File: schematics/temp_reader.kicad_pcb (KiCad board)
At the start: 2 copper layers, 54.5 x 53 mm, 11 parts, among them Q1 2N3904, Q2 2N3904, Q3 2N3904, U1 7-seg, U2 7-seg, U3 7-seg, U4 AM2320, U5 MG90S_servo

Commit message: added tempurature module
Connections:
- A1 pad 13: Net-(A1-D10) -> unconnected-(A1-D10-Pad13)
- A1 pad 2: Net-(A1-RX1) -> unconnected-(A1-RX1-Pad2)
- A1 pad 23: unconnected-(A1-SDA/A4-Pad23) -> SDA
- A1 pad 24: unconnected-(A1-SCL/A5-Pad24) -> SCL
- R1 pad 1: Net-(A1-D9) -> SCL
- R2 pad 1: Net-(A1-D10) -> SDA
- U4 pad 2: Net-(A1-D10) -> SDA
- U4 pad 4: Net-(A1-D9) -> SCL
- U5 pad 3: Net-(A1-RX1) -> Net-(A1-D9)
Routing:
- net Net-(A1-D10): track 81.5 -> 0.00 mm
- net SDA: track 0.00 -> 80.8 mm
- net SCL: track 0.00 -> 77.7 mm
- net Net-(A1-RX1): track 39.0 -> 0.00 mm
- net Net-(A1-D9): track 81.8 -> 72.0 mm
- net +5V: track 82.5 -> 84.6 mm, vias 3 -> 2
- net GND: track 87.0 -> 87.9 mm

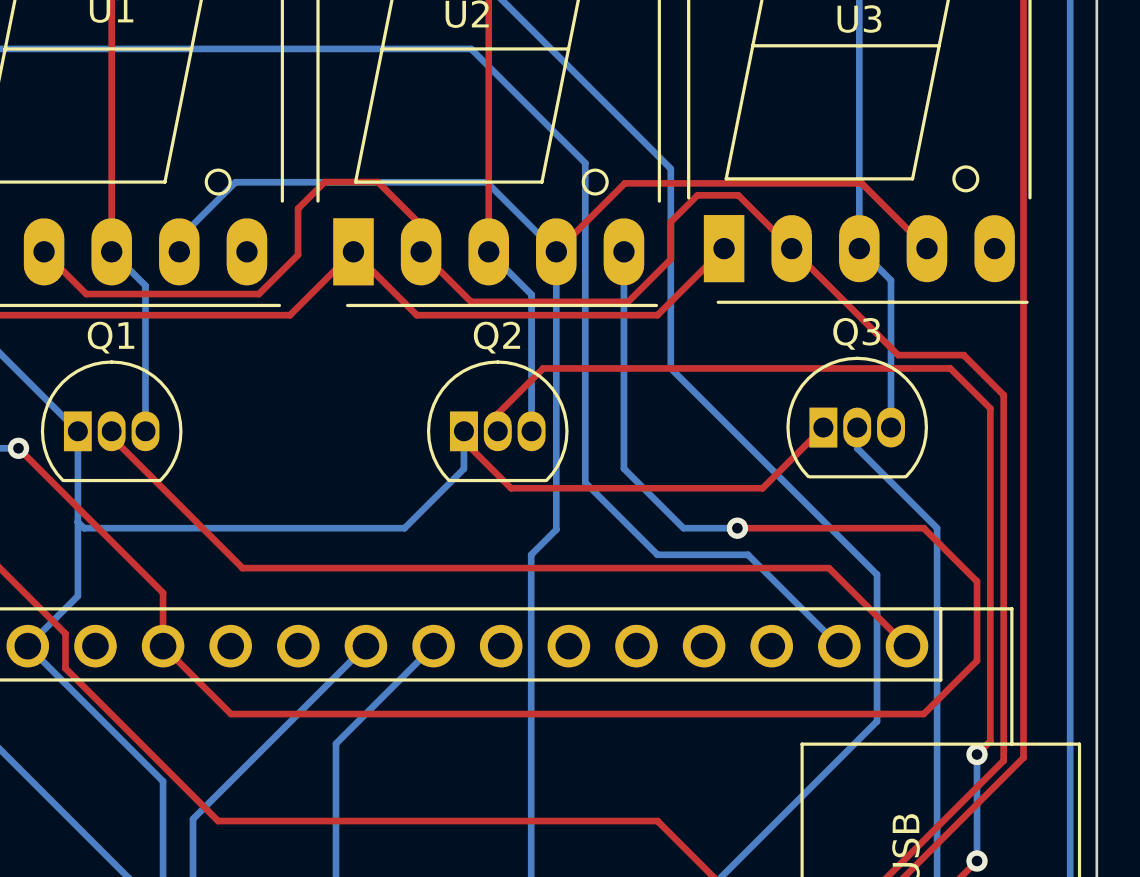
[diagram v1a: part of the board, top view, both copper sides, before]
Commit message: using 3.3v for decimal LED
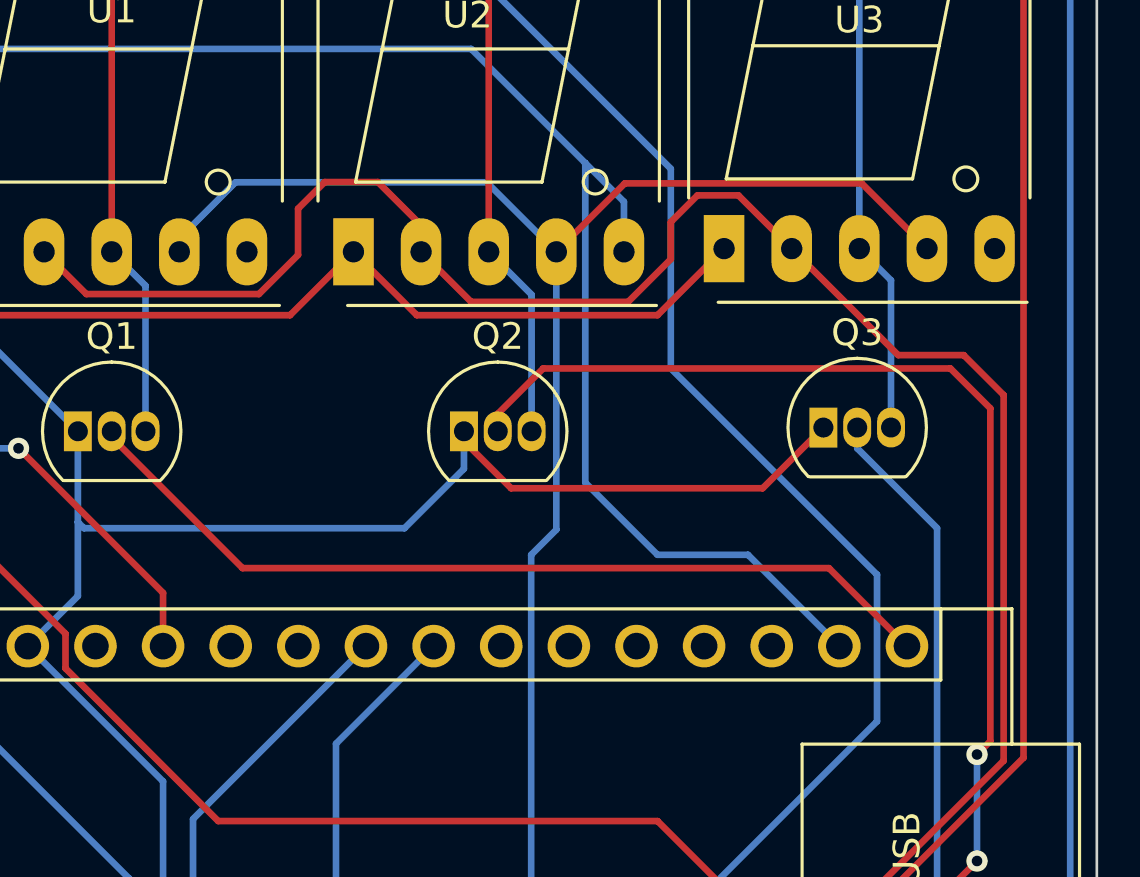
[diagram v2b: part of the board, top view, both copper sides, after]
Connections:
- U2 pad 5: +5V -> +3.3V
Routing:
- net +5V: track 84.6 -> 26.0 mm, vias 2 -> 1
- net +3.3V: track 87.3 -> 91.2 mm
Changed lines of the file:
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@@
       (net 23 "vbr") (pinfunction "vbr") (pintype "input"))
     (pad "5" thru_hole oval (at 0 10.16) (size 1.524 2.524) (drill 0.8) (layers "*.Cu" "*.Mask")
-      (net 26 "+5V") (pinfunction "DP") (pintype "input"))
+      (net 27 "+3.3V") (pinfunction "DP") (pintype "input"))
     (pad "6" thru_hole oval (at 15.24 10.16) (size 1.524 2.524) (drill 0.8) (layers "*.Cu" "*.Mask")
       (net 30 "vtr") (pinfunction "vtr") (pintype "input"))
@@
   (segment (start 145.58 76.62) (end 147.96 79) (width 0.25) (layer "F.Cu") (net 25))
   (segment (start 152.5 107.5) (end 153 108) (width 0.25) (layer "F.Cu") (net 25))
-  (segment (start 169 91.98) (end 169 89) (width 0.25) (layer "F.Cu") (net 26))
   (segment (start 138.43 89.43) (end 133 84) (width 0.25) (layer "F.Cu") (net 26))
-  (segment (start 140.98 93.98) (end 167 93.98) (width 0.25) (layer "F.Cu") (net 26))
   (segment (start 138.43 91.43) (end 138.43 89.43) (width 0.25) (layer "F.Cu") (net 26))
-  (segment (start 167 93.98) (end 169 91.98) (width 0.25) (layer "F.Cu") (net 26))
-  (segment (start 169 89) (end 167 87) (width 0.25) (layer "F.Cu") (net 26))
-  (segment (start 138.43 91.43) (end 140.98 93.98) (width 0.25) (layer "F.Cu") (net 26))
-  (segment (start 160 87) (end 167 87) (width 0.25) (layer "F.Cu") (net 26))
   (via (at 133 84) (size 0.8) (drill 0.4) (layers "F.Cu" "B.Cu") (net 26))
-  (via (at 160 87) (size 0.8) (drill 0.4) (layers "F.Cu" "B.Cu") (net 26))
   (segment (start 122.925 81.925) (end 122.925 78.075) (width 0.25) (layer "B.Cu") (net 26))
   (segment (start 122.925 78.075) (end 124 77) (width 0.25) (layer "B.Cu") (net 26))
-  (segment (start 155.74 76.62) (end 155.74 84.765305) (width 0.25) (layer "B.Cu") (net 26))
   (segment (start 133 84) (end 125 84) (width 0.25) (layer "B.Cu") (net 26))
   (segment (start 125 84) (end 122.925 81.925) (width 0.25) (layer "B.Cu") (net 26))
-  (segment (start 160 87) (end 158 87) (width 0.25) (layer "B.Cu") (net 26))
-  (segment (start 155.74 84.765305) (end 157.974695 87) (width 0.25) (layer "B.Cu") (net 26))
   (segment (start 123 85.5) (end 122 84.5) (width 0.25) (layer "F.Cu") (net 27))
   (segment (start 124.075 96.425) (end 124.075 88.075) (width 0.25) (layer "F.Cu") (net 27))
@@
   (segment (start 150 69) (end 154.287 73.287) (width 0.25) (layer "B.Cu") (net 27))
   (segment (start 154.287 85.287) (end 157 88) (width 0.25) (layer "B.Cu") (net 27))
+  (segment (start 154.287 73.287) (end 155.74 74.74) (width 0.25) (layer "B.Cu") (net 27))
   (segment (start 157 88) (end 160.4 88) (width 0.25) (layer "B.Cu") (net 27))
+  (segment (start 155.74 74.74) (end 155.74 76.62) (width 0.25) (layer "B.Cu") (net 27))
   (segment (start 160.4 88) (end 163.83 91.43) (width 0.25) (layer "B.Cu") (net 27))
   (segment (start 124 69) (end 150 69) (width 0.25) (layer "B.Cu") (net 27))

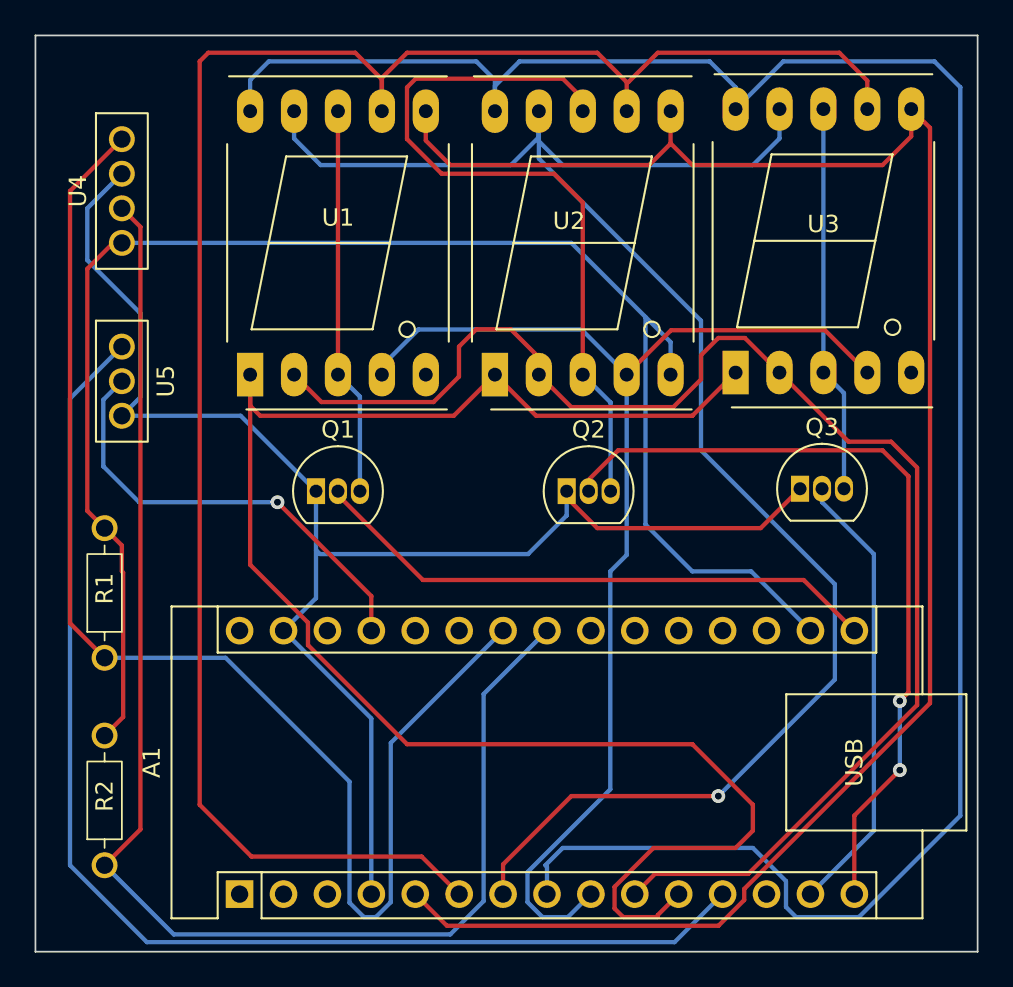
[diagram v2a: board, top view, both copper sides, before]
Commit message: updated servo model and adjusted temp sensor blueprint
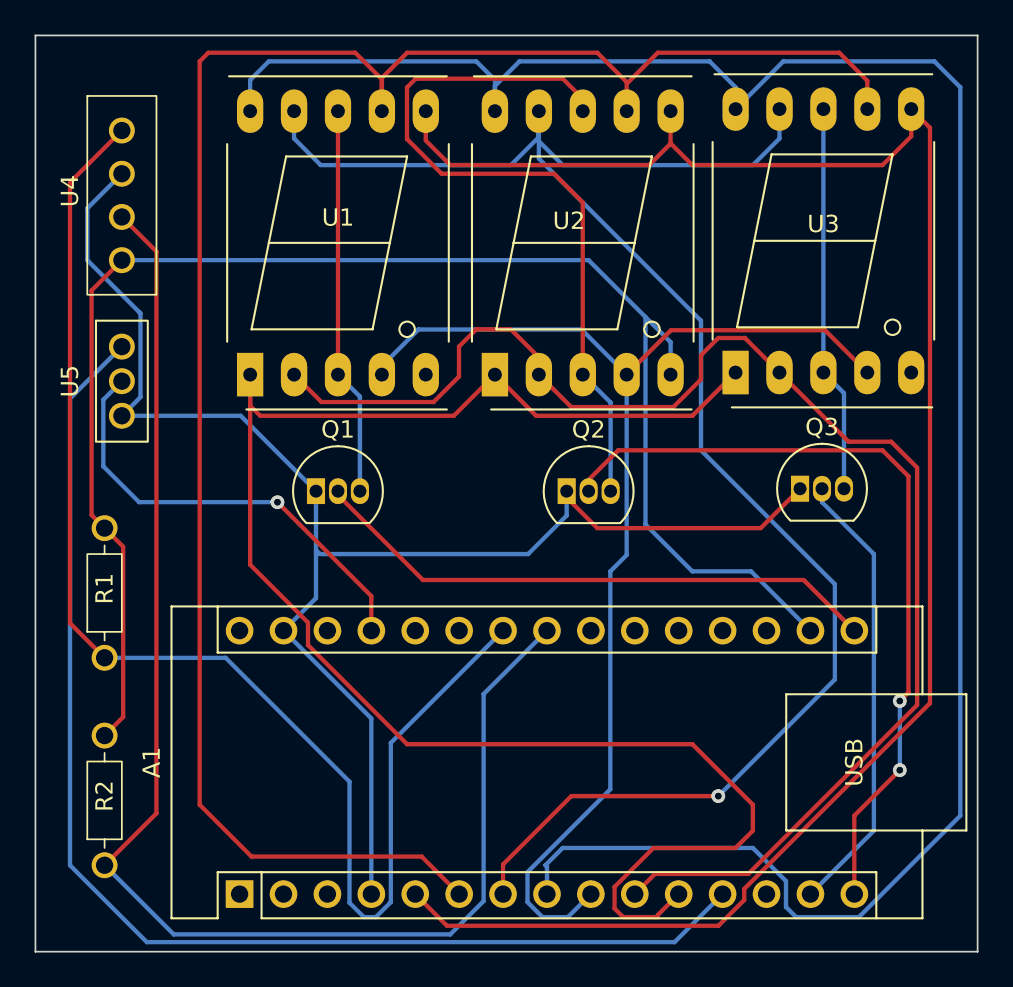
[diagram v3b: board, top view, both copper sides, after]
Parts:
- U5: value MG90S_servo -> SG90_servo
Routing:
- net +3.3V: track 91.2 -> 89.1 mm
- net SCL: track 77.7 -> 78.2 mm
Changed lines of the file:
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@@
     (property "Sheetname" "")
     (attr through_hole)
-    (fp_text reference "U5" (at 0 2.54 90 unlocked) (layer "F.SilkS")
-        (effects (font (size 1 1) (thickness 0.15)))
-    )
-    (fp_text value "MG90S_servo" (at 0 -2.5 90 unlocked) (layer "F.Fab")
+    (fp_text reference "U5" (at 0 -3 90 unlocked) (layer "F.SilkS")
+        (effects (font (size 1 1) (thickness 0.15)))
+    )
+    (fp_text value "SG90_servo" (at 0 -2.5 90 unlocked) (layer "F.Fab")
         (effects (font (size 1 1) (thickness 0.15)))
     )
@@
     (property "Sheetname" "")
     (attr through_hole)
-    (fp_text reference "U4" (at 0 -2.54 90 unlocked) (layer "F.SilkS")
+    (fp_text reference "U4" (at 0 -3 90 unlocked) (layer "F.SilkS")
         (effects (font (size 1 1) (thickness 0.15)))
     )
@@
         (effects (font (size 1 1) (thickness 0.15)))
     )
-    (fp_rect (start 4.5 -1.5) (end -4.5 1.5)
-      (stroke (width 0.12) (type solid)) (fill none) (layer "F.SilkS"))
-    (pad "1" thru_hole circle (at -3 0 90) (size 1.5 1.5) (drill 1) (layers "*.Cu" "*.Mask")
+    (fp_rect (start 5.5 -2) (end -6 2)
+      (stroke (width 0.1) (type default)) (fill none) (layer "F.SilkS"))
+    (pad "1" thru_hole circle (at -4 0 90) (size 1.5 1.5) (drill 1) (layers "*.Cu" "*.Mask")
       (net 27 "+3.3V") (pinfunction "V+") (pintype "input"))
-    (pad "2" thru_hole circle (at -1 0 90) (size 1.5 1.5) (drill 1) (layers "*.Cu" "*.Mask")
+    (pad "2" thru_hole circle (at -1.5 0 90) (size 1.5 1.5) (drill 1) (layers "*.Cu" "*.Mask")
       (net 11 "SDA") (pinfunction "SDA") (pintype "input"))
     (pad "3" thru_hole circle (at 1 0 90) (size 1.5 1.5) (drill 1) (layers "*.Cu" "*.Mask")
       (net 18 "GND") (pinfunction "GND") (pintype "input"))
-    (pad "4" thru_hole circle (at 3 0 90) (size 1.5 1.5) (drill 1) (layers "*.Cu" "*.Mask")
+    (pad "4" thru_hole circle (at 3.5 0 90) (size 1.5 1.5) (drill 1) (layers "*.Cu" "*.Mask")
       (net 12 "SCL") (pinfunction "SCL") (pintype "input"))
   )
@@
   (segment (start 121 105) (end 121 78) (width 0.25) (layer "B.Cu") (net 4))
   (segment (start 125.45 109.45) (end 121 105) (width 0.25) (layer "B.Cu") (net 4))
-  (segment (start 123 105) (end 125.075 102.925) (width 0.25) (layer "F.Cu") (net 11))
-  (segment (start 125.075 102.925) (end 125.075 68.075) (width 0.25) (layer "F.Cu") (net 11))
-  (segment (start 125.075 68.075) (end 124 67) (width 0.25) (layer "F.Cu") (net 11))
+  (segment (start 124 67.5) (end 126 69.5) (width 0.25) (layer "F.Cu") (net 11))
+  (segment (start 123 105) (end 126 102) (width 0.25) (layer "F.Cu") (net 11))
+  (segment (start 126 69.5) (end 126 102) (width 0.25) (layer "F.Cu") (net 11))
   (segment (start 144.925 95.095) (end 144.925 107.075) (width 0.25) (layer "B.Cu") (net 11))
   (segment (start 127 109) (end 123 105) (width 0.25) (layer "B.Cu") (net 11))
@@
   (segment (start 143 109) (end 127 109) (width 0.25) (layer "B.Cu") (net 11))
   (segment (start 148.59 91.43) (end 144.925 95.095) (width 0.25) (layer "B.Cu") (net 11))
-  (segment (start 124 63) (end 121 66) (width 0.25) (layer "F.Cu") (net 12))
+  (segment (start 121 65.5) (end 121 91) (width 0.25) (layer "F.Cu") (net 12))
+  (segment (start 124 62.5) (end 121 65.5) (width 0.25) (layer "F.Cu") (net 12))
   (segment (start 121 91) (end 123 93) (width 0.25) (layer "F.Cu") (net 12))
-  (segment (start 121 66) (end 121 91) (width 0.25) (layer "F.Cu") (net 12))
   (segment (start 139.555 97.925) (end 146.05 91.43) (width 0.25) (layer "B.Cu") (net 12))
   (segment (start 138 108) (end 138.690991 108) (width 0.25) (layer "B.Cu") (net 12))
@@
   (segment (start 133 84) (end 125 84) (width 0.25) (layer "B.Cu") (net 26))
   (segment (start 125 84) (end 122.925 81.925) (width 0.25) (layer "B.Cu") (net 26))
-  (segment (start 123 85.5) (end 122 84.5) (width 0.25) (layer "F.Cu") (net 27))
-  (segment (start 124.075 96.425) (end 124.075 88.075) (width 0.25) (layer "F.Cu") (net 27))
+  (segment (start 124 70) (end 122.25 71.75) (width 0.25) (layer "F.Cu") (net 27))
+  (segment (start 122.25 71.75) (end 122.25 84.75) (width 0.25) (layer "F.Cu") (net 27))
+  (segment (start 124.075 86.575) (end 123 85.5) (width 0.25) (layer "F.Cu") (net 27))
+  (segment (start 122.25 84.75) (end 123 85.5) (width 0.25) (layer "F.Cu") (net 27))
+  (segment (start 124.075 96.425) (end 124.075 86.575) (width 0.25) (layer "F.Cu") (net 27))
   (segment (start 123 97.5) (end 124.075 96.425) (width 0.25) (layer "F.Cu") (net 27))
-  (segment (start 122 84.5) (end 122 70.5) (width 0.25) (layer "F.Cu") (net 27))
-  (segment (start 124 88) (end 124 86.5) (width 0.25) (layer "F.Cu") (net 27))
-  (segment (start 124 86.5) (end 123 85.5) (width 0.25) (layer "F.Cu") (net 27))
-  (segment (start 122 70.5) (end 124 68.5) (width 0.25) (layer "F.Cu") (net 27))
-  (segment (start 124.075 88.075) (end 124 88) (width 0.25) (layer "F.Cu") (net 27))
-  (segment (start 150 69) (end 154.287 73.287) (width 0.25) (layer "B.Cu") (net 27))
   (segment (start 154.287 85.287) (end 157 88) (width 0.25) (layer "B.Cu") (net 27))
   (segment (start 154.287 73.287) (end 155.74 74.74) (width 0.25) (layer "B.Cu") (net 27))
@@
   (segment (start 155.74 74.74) (end 155.74 76.62) (width 0.25) (layer "B.Cu") (net 27))
   (segment (start 160.4 88) (end 163.83 91.43) (width 0.25) (layer "B.Cu") (net 27))
-  (segment (start 124 69) (end 150 69) (width 0.25) (layer "B.Cu") (net 27))
+  (segment (start 154.287 73.287) (end 151 70) (width 0.25) (layer "B.Cu") (net 27))
   (segment (start 154.287 73.287) (end 154.287 85.287) (width 0.25) (layer "B.Cu") (net 27))
+  (segment (start 151 70) (end 124 70) (width 0.25) (layer "B.Cu") (net 27))
   (segment (start 142.5 65) (end 149 65) (width 0.25) (layer "F.Cu") (net 28))
   (segment (start 149 65) (end 150.66 66.66) (width 0.25) (layer "F.Cu") (net 28))

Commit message: reorganized PCB layout to move sensor farther away from displays
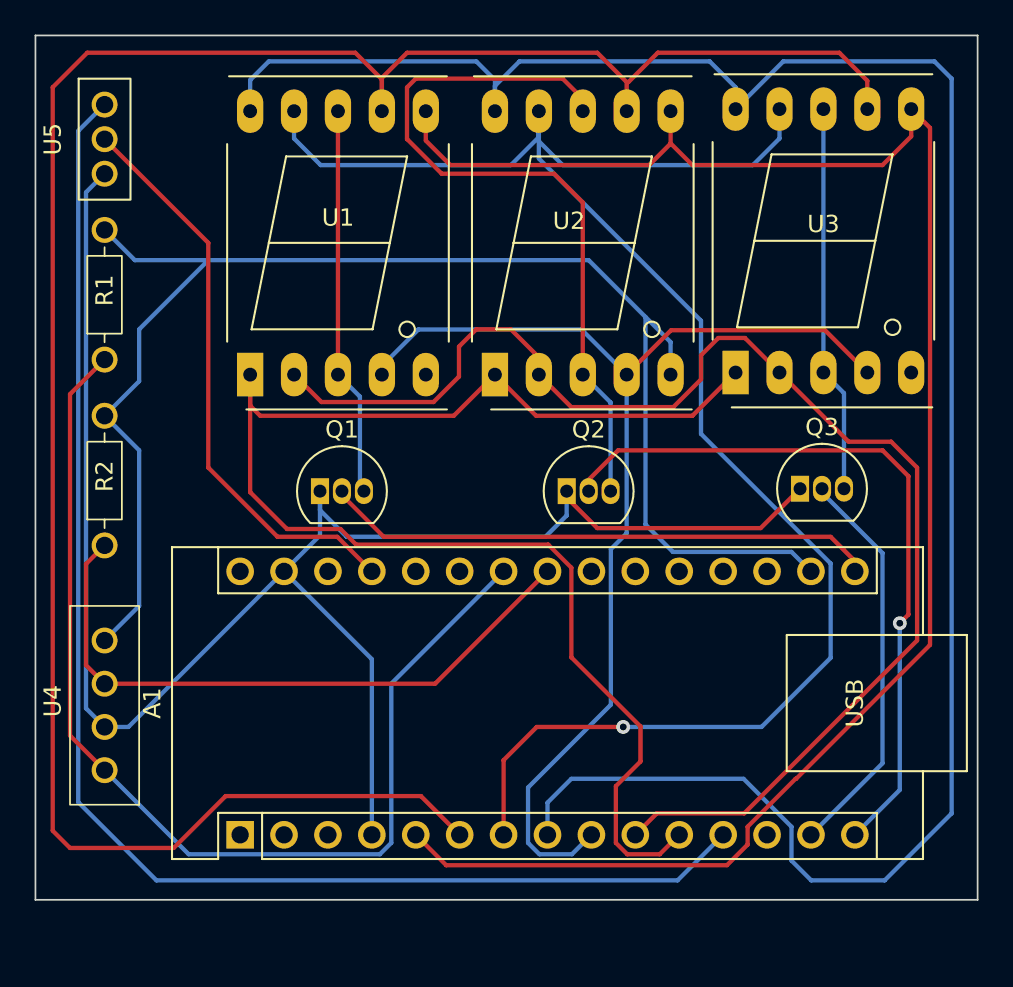
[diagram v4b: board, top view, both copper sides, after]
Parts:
- moved U4 30.0 mm to (123.0, 96.0), turned to -90 degrees
- moved R2 18.5 mm to (123.0, 86.5)
- moved R1 17.2 mm to (123.0, 75.8)
- moved U5 14.0 mm to (123.0, 63.0)
- moved A1 3.43 mm to (130.8, 103.2)
- moved Q1 0.23 mm to (135.5, 83.4)
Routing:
- net SDA: track 81.1 -> 37.2 mm
- net ht: track 109.4 -> 127.5 mm
- net SCL: track 78.2 -> 62.7 mm
- net GND: track 87.9 -> 102.9 mm
- net vbl: track 96.4 -> 82.9 mm
- net Net-(A1-D9): track 72.0 -> 81.3 mm
- net +5V: track 26.0 -> 33.4 mm, vias 1 -> 0
- net hb: track 81.1 -> 77.4 mm
- net vbr: track 69.6 -> 66.0 mm
- net seg2: track 45.9 -> 42.5 mm, vias 2 -> 1
- net vtr: track 106.6 -> 103.4 mm
- net seg3: track 26.2 -> 23.0 mm
- net +3.3V: track 89.1 -> 86.1 mm
- net seg1: track 33.1 -> 31.3 mm
- net vtl: track 102.4 -> 101.4 mm
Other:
- board size 54.5 x 53 mm -> 54.5 x 50 mm
